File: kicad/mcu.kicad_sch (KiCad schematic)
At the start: 28 parts, among them J201 SWD, SW201 RESET, SW202 BOOT, U200 STM32F407VET6, U201 REF3030, Y201 8MHz 20pF

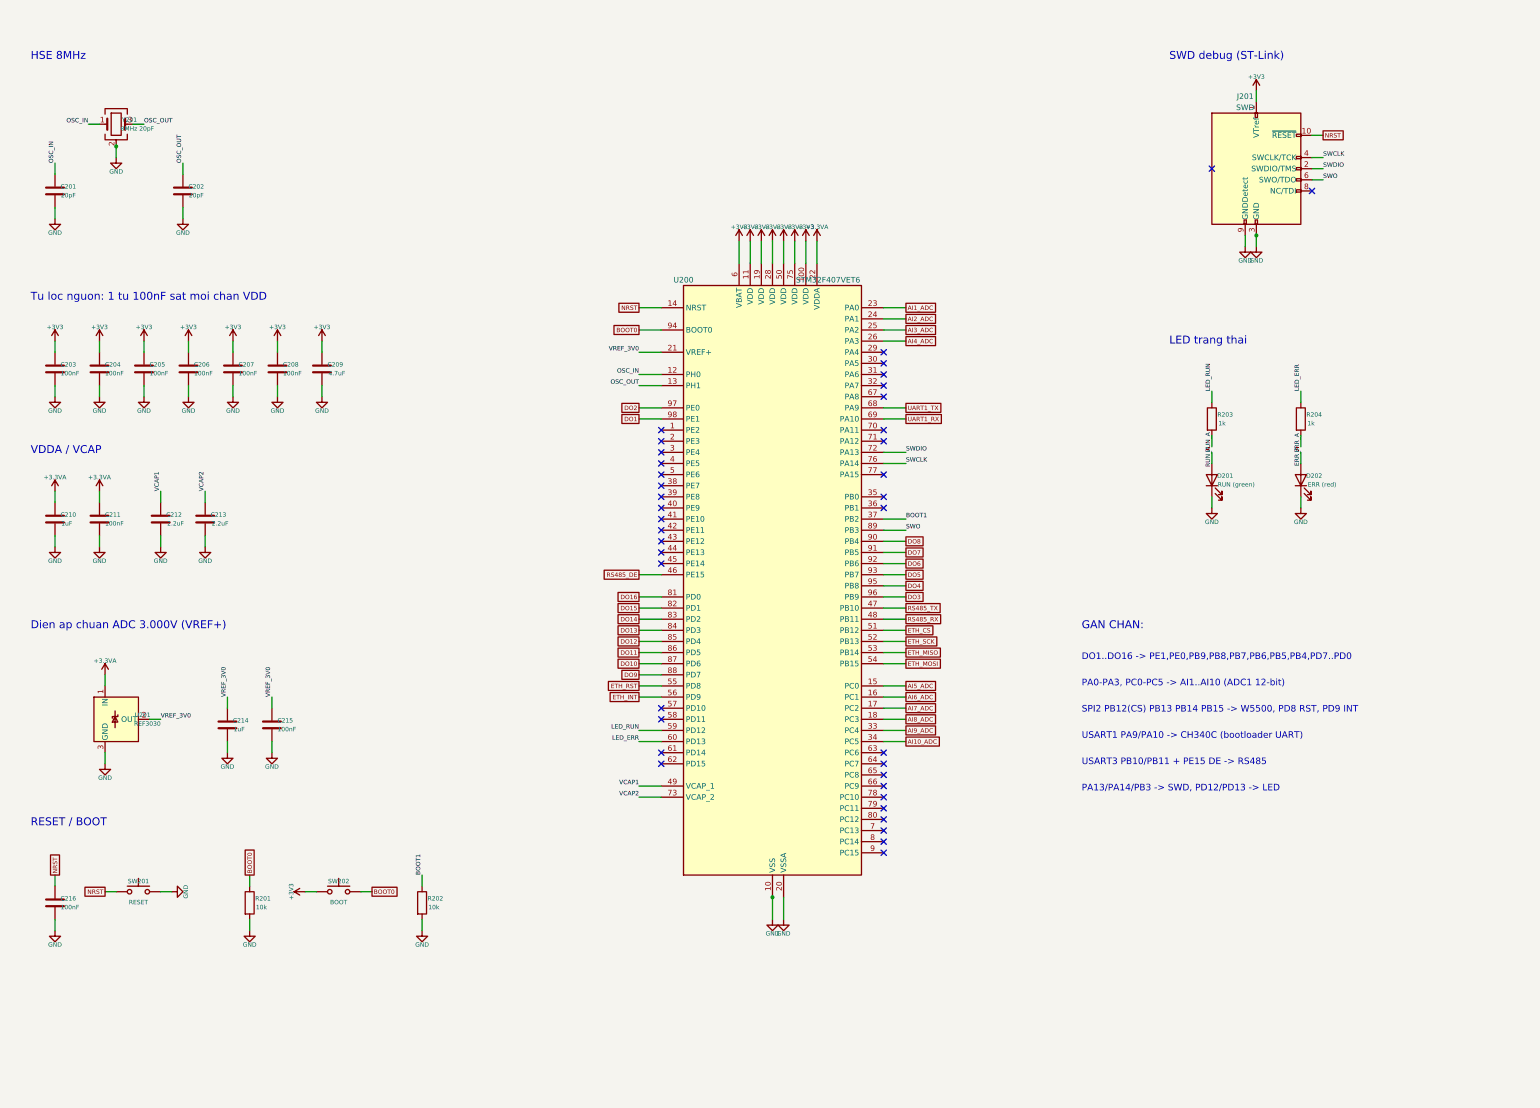
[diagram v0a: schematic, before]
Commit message: - bỏ các mạch 0-10v, RS485 RTU
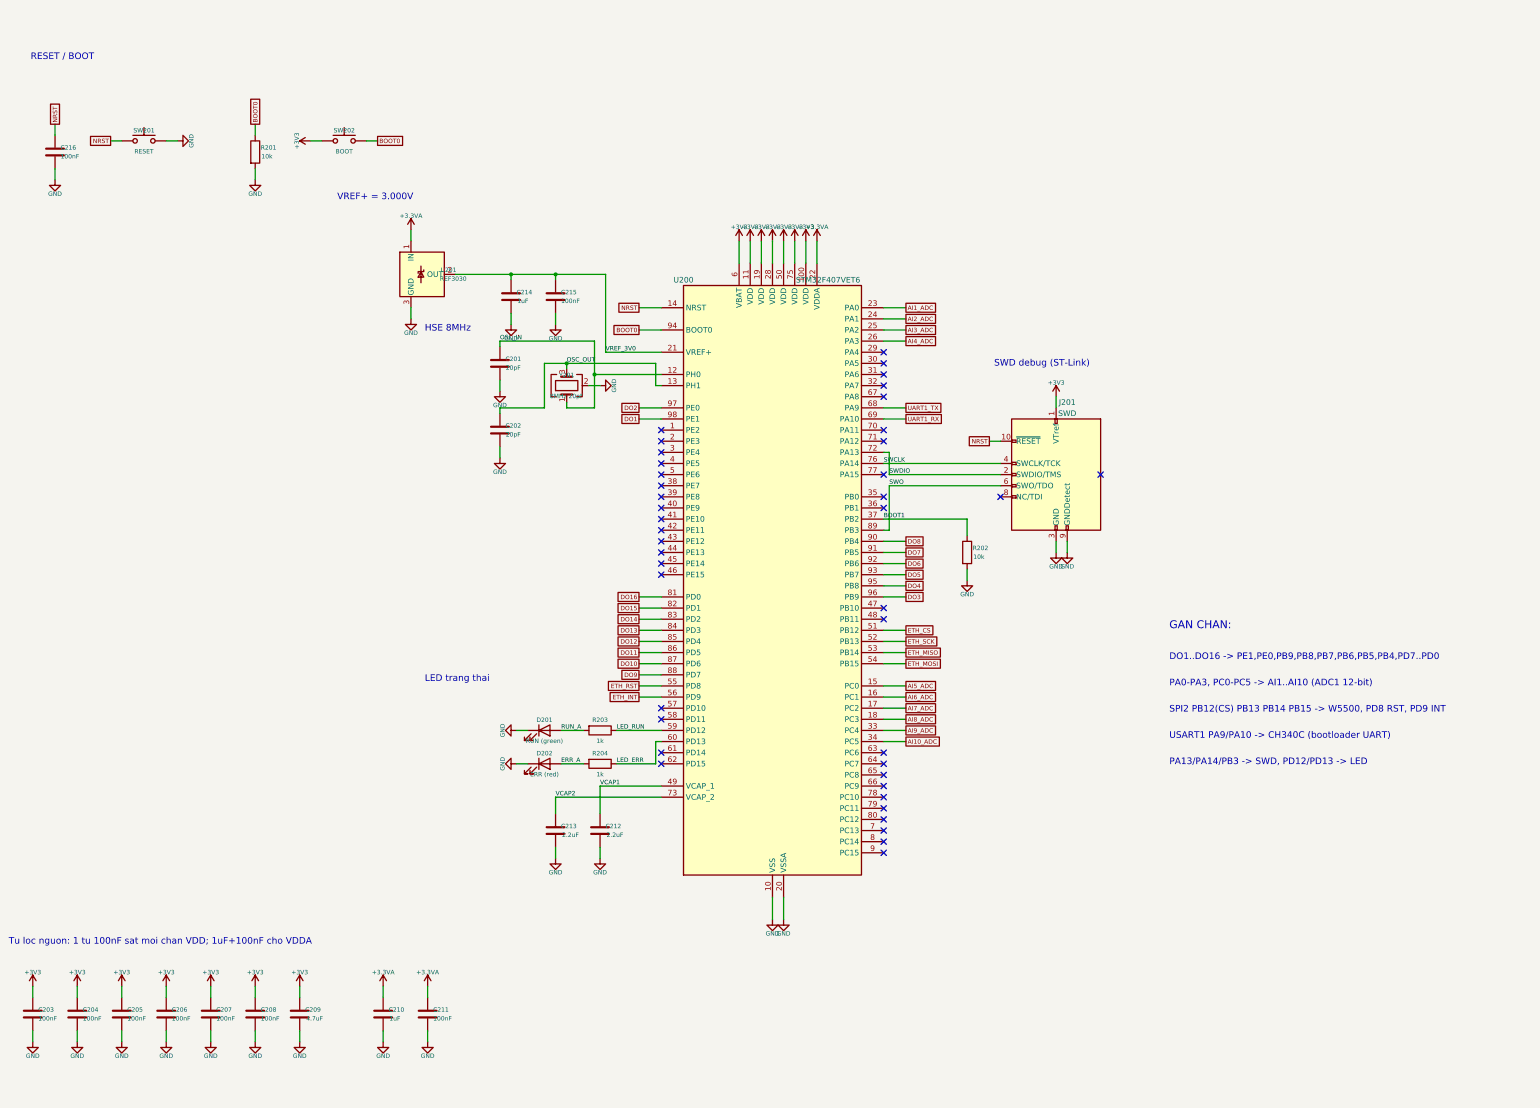
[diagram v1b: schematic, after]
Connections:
- net RS485_DE: no longer names the net of U200.46 (PE15)
- net RS485_RX: no longer names the net of U200.48 (PB11)
- net RS485_TX: no longer names the net of U200.47 (PB10)
- no-connect marks 39 -> 42
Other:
- note added: "Tu loc nguon: 1 tu 100nF sat moi chan VDD; 1uF+100nF cho VDDA"
- note added: "VREF+ = 3.000V"
- note removed: "Dien ap chuan ADC 3.000V (VREF+)"
- note removed: "Tu loc nguon: 1 tu 100nF sat moi chan VDD"
- note removed: "USART3 PB10/PB11 + PE15 DE -> RS485"
- note removed: "VDDA / VCAP"

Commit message: - bỏ các cầu chì thêm mô tả cho từng linh kiên
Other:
- note added: "BOOT0: R201 10k kéo xuống → chạy từ Flash. Giữ BOOT khi reset → BOOT0 = 1 → bootloader UART."
- note added: "BOOT1 (PB2) = 0 qua R202 10k → chọn bootloader hệ thống."
- note added: "C203–C208 100nF: một tụ cho mỗi chân VDD, đặt sát chân trên PCB. C209 4.7µF: dự trữ chung (ST AN4488)."
- note added: "DO1–16: PE1, PE0, PB9…PB4, PD7…PD0 • AI1–10: PA0–PA3, PC0–PC5 • SPI2 → W5500 • USART1 → CH340."
- note added: "LED RUN/ERR: I = (3.3V − 2.0V)/1kΩ ≈ 1.3mA (GPIO ≤ 25mA)."
- note added: "NRST: C216 100nF lọc nhiễu + nút RESET (trở kéo lên 40k có sẵn trong chip)."
- note added: "REF3030: VREF+ = 3.000V ±0.2% → 1 LSB = 3.0V/4096 ≈ 0.73mV. C214 1µF + C215 100nF giữ ổn định."
- note added: "STM32F407VET6 (168MHz, Flash 512KB, RAM 192KB)"
- note added: "SWD (ST-Link): nạp và gỡ lỗi; VTref báo mức 3.3V."
- note added: "VCAP 2.2µF ESR thấp: bắt buộc cho ổn áp 1.2V của lõi (datasheet)."
- note added: "VDDA: C210 1µF + C211 100nF – nguồn sạch cho ADC."
- note added: "Y201 8MHz → PLL 168MHz. Tụ tải C = 2·(C_L − C_stray) = 2 × (12 − 2) = 20pF (C_L theo datasheet thạch anh)."
